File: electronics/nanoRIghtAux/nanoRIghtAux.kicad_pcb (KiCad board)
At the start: 2 copper layers, 87.6 x 71.1 mm, 22 parts, among them J1 Conn_MM5451, J10 Conn_EA_GLCD, J11 Conn_MAX7219, J12 Conn_PWRInput, J13 Conn_MAX_Pwr, J2 Conn_HYDA, J3 Conn_HYDB, J4 Conn_FUEL_FR, J5 Conn_FUEL_AL, J6 Conn_MOT_D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

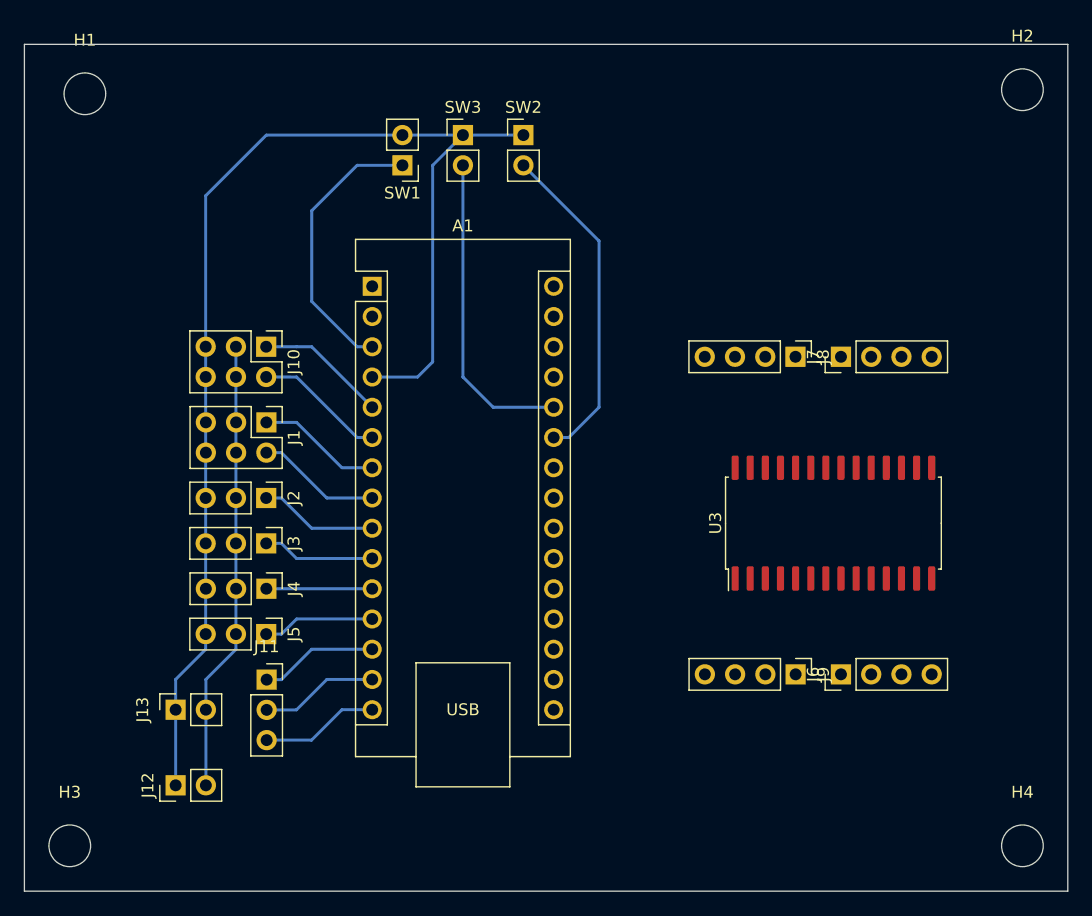
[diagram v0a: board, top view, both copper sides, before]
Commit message: changed footprint of AX12 to DIP28
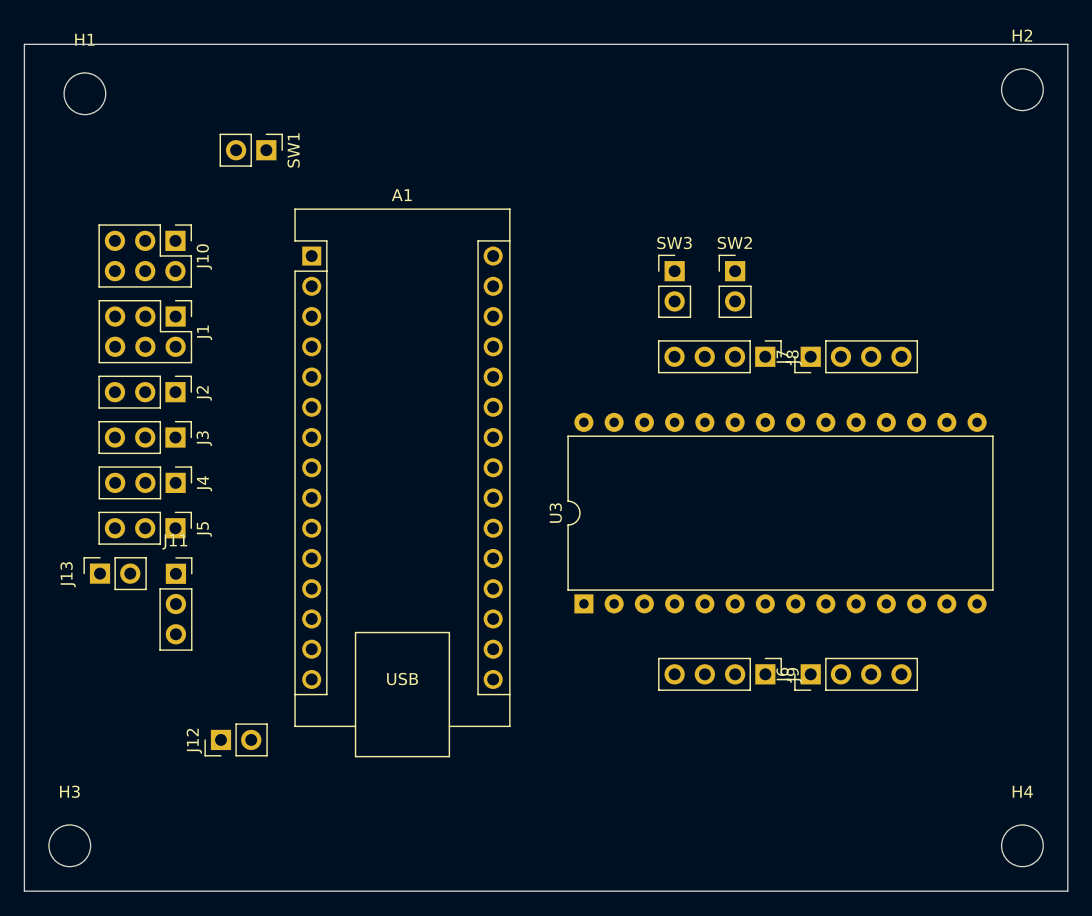
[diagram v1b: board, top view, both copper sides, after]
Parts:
- U3: footprint Package_SO:SOIC-28W_7.5x17.9mm_P1.27mm -> Package_DIP:DIP-28_W15.24mm
- moved U3 22.0 mm to (181.6, 106.7)
- moved SW2 21.1 mm to (194.3, 78.7)
- moved SW3 21.1 mm to (189.2, 78.7)
- moved J13 13.1 mm to (141.0, 104.1)
- moved J1 11.7 mm to (147.3, 82.5)
- moved J10 11.7 mm to (147.3, 76.2)
- moved J11 11.7 mm to (147.3, 104.2)
- moved J2 11.7 mm to (147.3, 88.9)
- moved J3 11.7 mm to (147.3, 92.7)
- moved J4 11.7 mm to (147.3, 96.5)
- moved J5 11.7 mm to (147.3, 100.3)
- moved SW1 11.5 mm to (154.9, 68.6), turned to -90 degrees
- moved A1 5.68 mm to (158.8, 77.5)
- moved J12 5.39 mm to (151.1, 118.1)
- moved J6 2.54 mm to (200.7, 112.6)
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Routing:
- net GND: track 105.1 -> 0.00 mm
- net +5V: track 37.9 -> 0.00 mm
- net Net-(A1-A6): track 27.8 -> 0.00 mm
- net Net-(A1-A7): track 26.5 -> 0.00 mm
- net Net-(A1-~{RESET}-Pad3): track 23.5 -> 0.00 mm
- net Net-(A1-D3): track 11.0 -> 0.00 mm
- net Net-(A1-D2): track 11.0 -> 0.00 mm
- net Net-(A1-D5): track 10.5 -> 0.00 mm
- net Net-(A1-D4): track 10.5 -> 0.00 mm
- net Net-(A1-D6): track 9.96 -> 0.00 mm
- net Net-(A1-D12): track 9.92 -> 0.00 mm
- net Net-(A1-D10): track 9.92 -> 0.00 mm
- net Net-(A1-D11): track 9.92 -> 0.00 mm
- net Net-(A1-D7): track 9.43 -> 0.00 mm
- net Net-(A1-D9): track 9.43 -> 0.00 mm
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
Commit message: changed pin assignments for AX12 to facilitate routing
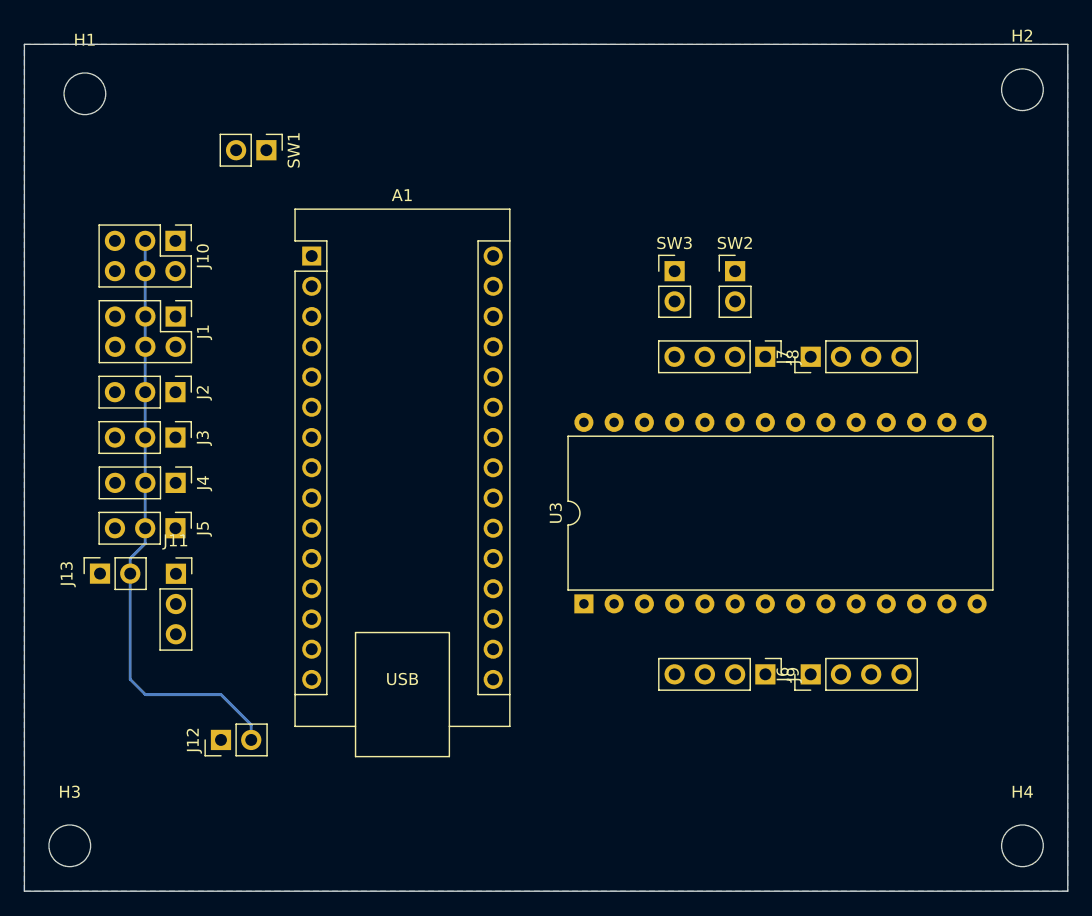
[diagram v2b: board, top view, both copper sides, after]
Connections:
- U3 pad 13: Net-(A1-A0) -> Net-(A1-A1)
- U3 pad 14: Net-(A1-A1) -> Net-(A1-A2)
- U3 pad 2: Net-(A1-A2) -> Net-(A1-A0)
- U3 pad 26: Net-(A1-D13) -> Net-(A1-A3)
- U3 pad 3: Net-(A1-A3) -> Net-(A1-D13)
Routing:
- net +5V: track 0.00 -> 50.4 mm
- added copper zone on B.Cu, net GND

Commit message: new routing started, 12mm hole for placint GX12 connector added
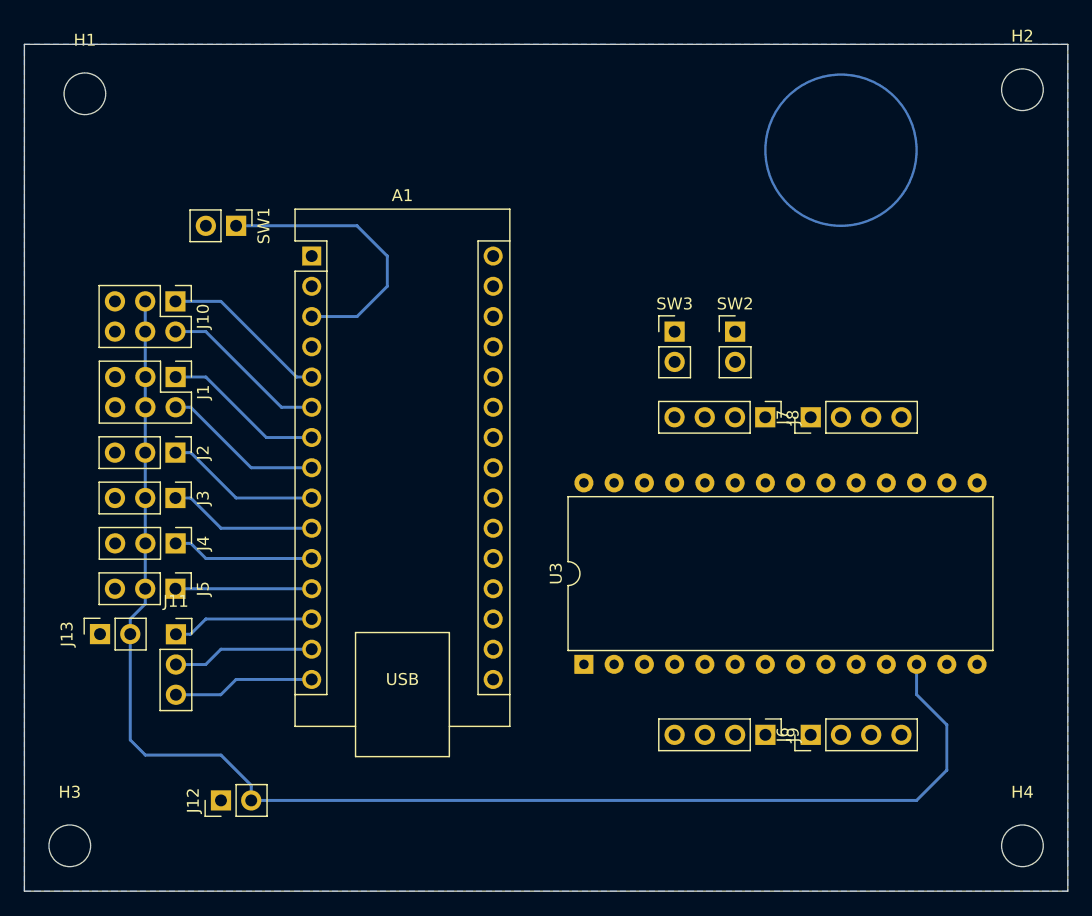
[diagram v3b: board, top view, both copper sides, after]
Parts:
- moved SW1 6.84 mm to (152.4, 74.9)
- moved J10 5.08 mm to (147.3, 81.3)
- moved J3 5.08 mm to (147.3, 97.8)
- moved J6 5.08 mm to (200.7, 117.7)
- moved J9 5.08 mm to (196.8, 117.7)
- moved J1 5.08 mm to (147.3, 87.6)
- moved J11 5.08 mm to (147.3, 109.2)
- moved J12 5.08 mm to (151.1, 123.2)
- moved J13 5.08 mm to (141.0, 109.2)
- moved J2 5.08 mm to (147.3, 94.0)
- moved J4 5.08 mm to (147.3, 101.6)
- moved J5 5.08 mm to (147.3, 105.4)
- moved J7 5.08 mm to (200.7, 91.0)
- moved J8 5.08 mm to (196.8, 91.0)
- moved SW2 5.08 mm to (194.3, 83.8)
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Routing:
- net +5V: track 50.4 -> 119.8 mm
- net Net-(A1-~{RESET}-Pad3): track 0.00 -> 23.7 mm
- net Net-(A1-D3): track 0.00 -> 14.1 mm
- net Net-(A1-D2): track 0.00 -> 14.1 mm
- net Net-(A1-D5): track 0.00 -> 13.5 mm
- net Net-(A1-D4): track 0.00 -> 13.5 mm
- net Net-(A1-D6): track 0.00 -> 13.0 mm
- net Net-(A1-D7): track 0.00 -> 12.5 mm
- net Net-(A1-D8): track 0.00 -> 12.0 mm
- net Net-(A1-D11): track 0.00 -> 11.9 mm
- net Net-(A1-D12): track 0.00 -> 11.9 mm
- net Net-(A1-D10): track 0.00 -> 11.9 mm
- net Net-(A1-D9): track 0.00 -> 11.4 mm

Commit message: text on frontside added
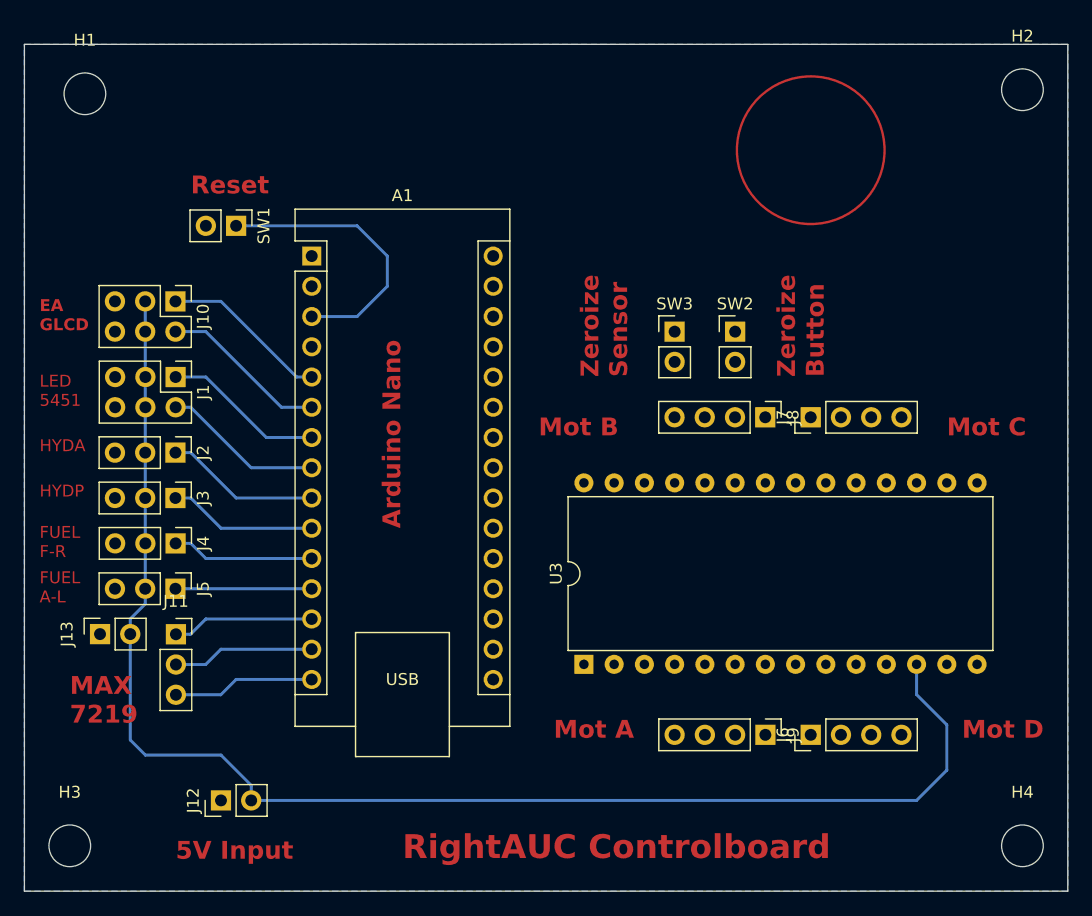
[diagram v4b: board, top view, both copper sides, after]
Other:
- board text added: "5V Input"
- board text added: "Arduino Nano"
- board text added: "EA GLCD"
- board text added: "FUEL A-L"
- board text added: "FUEL F-R"
- board text added: "HYDA"
- board text added: "HYDP"
- board text added: "LED 5451"
- board text added: "MAX 7219"
- board text added: "Mot A"
- board text added: "Mot B"
- board text added: "Mot C"
- board text added: "Mot D"
- board text added: "Reset"
- board text added: "RightAUC Controlboard"
- board text added: "Zeroize Button"
- board text added: "Zeroize Sensor"
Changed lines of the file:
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@@
     )
   )
-  (gr_circle (center 203.2 68.58) (end 207.01 73.66)
-    (stroke (width 0.2) (type default)) (fill none) (layer "B.Cu"))
+  (gr_circle (center 200.66 68.58) (end 206.86 68.58)
+    (stroke (width 0.2) (type default)) (fill none) (layer "F.Cu"))
   (gr_rect (start 134.62 59.69) (end 222.25 130.81)
     (stroke (width 0.1) (type default)) (fill none) (layer "Edge.Cuts"))
+  (gr_text "Mot D" (at 213.36 118.11) (layer "F.Cu")
+    (effects (font (size 1.5 1.5) (thickness 0.3) bold) (justify left bottom))
+  )
+  (gr_text "LED\n5451" (at 135.89 90.17) (layer "F.Cu")
+    (effects (font (size 1 1) (thickness 0.15)) (justify left bottom))
+  )
+  (gr_text "Mot C" (at 212.09 92.71) (layer "F.Cu")
+    (effects (font (size 1.5 1.5) (thickness 0.3) bold) (justify left bottom))
+  )
+  (gr_text "Mot A" (at 179.07 118.11) (layer "F.Cu")
+    (effects (font (size 1.5 1.5) (thickness 0.3) bold) (justify left bottom))
+  )
+  (gr_text "EA\nGLCD" (at 135.89 83.82) (layer "F.Cu")
+    (effects (font (size 1 1) (thickness 0.25) bold) (justify left bottom))
+  )
+  (gr_text "Arduino Nano" (at 166.37 100.33 90) (layer "F.Cu")
+    (effects (font (size 1.5 1.5) (thickness 0.3) bold) (justify left bottom))
+  )
+  (gr_text "Zeroize\nSensor" (at 185.42 87.63 90) (layer "F.Cu")
+    (effects (font (size 1.5 1.5) (thickness 0.3) bold) (justify left bottom))
+  )
+  (gr_text "Reset" (at 148.59 72.39) (layer "F.Cu")
+    (effects (font (size 1.5 1.5) (thickness 0.3) bold) (justify left bottom))
+  )
+  (gr_text "FUEL\nA-L" (at 135.89 106.68) (layer "F.Cu")
+    (effects (font (size 1 1) (thickness 0.15)) (justify left bottom))
+  )
+  (gr_text "HYDP" (at 135.89 97.79) (layer "F.Cu")
+    (effects (font (size 1 1) (thickness 0.15)) (justify left bottom))
+  )
+  (gr_text "Zeroize\nButton" (at 201.93 87.63 90) (layer "F.Cu")
+    (effects (font (size 1.5 1.5) (thickness 0.3) bold) (justify left bottom))
+  )
+  (gr_text "RightAUC Controlboard" (at 166.37 128.27) (layer "F.Cu")
+    (effects (font (size 2 2) (thickness 0.3) bold) (justify left bottom))
+  )
+  (gr_text "HYDA" (at 135.89 93.98) (layer "F.Cu")
+    (effects (font (size 1 1) (thickness 0.15)) (justify left bottom))
+  )
+  (gr_text "FUEL\nF-R" (at 135.89 102.87) (layer "F.Cu")
+    (effects (font (size 1 1) (thickness 0.15)) (justify left bottom))
+  )
+  (gr_text "5V Input" (at 147.32 128.27) (layer "F.Cu")
+    (effects (font (size 1.5 1.5) (thickness 0.3) bold) (justify left bottom))
+  )
+  (gr_text "MAX\n7219" (at 138.43 116.84) (layer "F.Cu")
+    (effects (font (size 1.5 1.5) (thickness 0.3) bold) (justify left bottom))
+  )
+  (gr_text "Mot B" (at 177.8 92.71) (layer "F.Cu")
+    (effects (font (size 1.5 1.5) (thickness 0.3) bold) (justify left bottom))
+  )
   (gr_text "RightAUX Control Board" (at 196.85 127) (layer "B.SilkS")
     (effects (font (size 2 2) (thickness 0.15)) (justify left bottom mirror))
